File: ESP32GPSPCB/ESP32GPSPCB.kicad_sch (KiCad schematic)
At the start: 11 parts, among them J1 Conn_01x04_Socket, U1 NEO-M8N, U2 W25Q16JVSS, U4 AP2112K-3.3

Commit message: completed GPS and BUCK-BOOST CONV
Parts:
- removed U2: W25Q16JVSS, Package_SO:SOIC-8_5.3x5.3mm_P1.27mm, symbol Memory_Flash:W25Q16JVSS
- added AE1: Antenna, symbol Device:Antenna
- added C4: 470nF, symbol Device:C
- added C5, C6, C7: 10uF, symbol Device:C
- added C8: 100nF, symbol Device:C
- added D2: FIX_IND-LED, symbol Device:LED
- added D3: D, symbol Device:D
- added D4, D5: LED, symbol Device:LED
- added J2: USB_C_Receptacle_USB2.0_14P, symbol Connector:USB_C_Receptacle_USB2.0_14P
- added L1: 27uH, symbol Device:L
- added R10, R11, R3: 1k, symbol Device:R
- added R12: 10mΩ, symbol Device:R
- added R13, R14: 4.7k, symbol Device:R
- added R15: 10K, symbol Device:R
- added R4, R9: 10k, symbol Device:R
- added R5: 22R, symbol Device:R
- added R6, R7: 5.1k, symbol Device:R
- added R8: 2K, symbol Device:R
- added U2: MCP73871-2AA, Package_DFN_QFN:QFN-20-1EP_4x4mm_P0.5mm_EP2.5x2.5mm, symbol Battery_Management:MCP73871-2AA
- added U5: MAX17261xxTD, Package_DFN_QFN:TDFN-14-1EP_3x3mm_P0.4mm_EP1.78x2.35mm, symbol Battery_Management:MAX17261xxTD
- BT1: value Battery_Cell -> CR2032
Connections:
- net +3V3: now also U1.14 (LNA_EN), D3.2 (A), R13.2, R14.2, R15.2, R4.1; no longer R2.2
- net +5V: now also J1.2 (Pin_2), C5.2, C6.2, J2.A4 (VBUS), J2.A9 (VBUS), J2.B4 (VBUS), J2.B9 (VBUS), R10.2, R11.2, R9.2, U2.17 (CE), U2.18 (IN), U2.19 (IN), U2.2 (VPCC), U2.9 (~{TE}); no longer J1.4 (Pin_4)
- net GND: now also U1.7 (VDD_USB), C4.2, C5.1, C6.1, C7.2, C8.1, D2.1 (K), J2.A1 (GND), J2.A12 (GND), J2.B1 (GND), J2.B12 (GND), J2.S1 (SHIELD), R12.1, R6.2, R7.1, R8.1, U2.10 (V_{SS}), U2.11 (V_{SS}), U2.12 (PROG3), U2.21 (V_{SS}), U2.3 (SEL), U2.4 (PROG2), U5.10 (CELLX), U5.15 (GND), U5.3 (SW), U5.8 (GND)
- net at U1.20 (TXD/SPI_MISO): now also J1.4 (Pin_4); no longer J1.2 (Pin_2)
- net at U1.11 (RF_IN): now also AE1.1 (A), L1.2
- net at U1.2 (D_SEL): now also R4.2
- net at U1.3 (TIMEPULSE): now also R3.1
- net at U1.9 (VCC_RF): now also R5.1
- new net: C4.1, U5.11 (REG)
- new net: J2.A5 (CC1), R6.1
- new net: J2.B5 (CC2), R7.2
- new net: R8.2, U2.13 (PROG1)
- new net: R9.1, U2.6 (~{PG})
- new net: D4.1 (K), U2.8 (STAT1/~{LBO})
- new net: D4.2 (A), R11.1
- new net: L1.1, R5.2
- new net: D3.1 (K), R2.2
- new net: R12.2, U5.7 (CSN)
- new net: D2.2 (A), R3.2
- new net: D5.2 (A), R10.1
- new net: D5.1 (K), U2.7 (STAT2)
- new net BAT_ALRT: R15.1, U5.12 (ALRT)
- new net D+: J2.A7 (D-), J2.B7 (D-)
- new net D-: J2.A6 (D+), J2.B6 (D+)
- new net I2C_SCL: R13.1, U5.14 (SCL)
- new net I2C_SDA: R14.1, U5.13 (SDA)
- new net VBAT: C7.1, C8.2, U2.14 (V_{BAT}), U2.15 (V_{BAT}), U2.16 (V_{BAT_SENSE}), U2.5 (THERM), U5.1 (TH), U5.6 (BATT), U5.9 (CSPL)
- new net VSYS: U2.1 (OUT), U2.20 (OUT)
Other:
- note added: "GPS MAPS"
- moved on the sheet: BT1, C1, C2, C3, D1, J1, R1, R2, U1, U4

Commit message: fixed some stuff
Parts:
- added C10, C9: 22uF, symbol Device:C
- added C11: 0.1uF, symbol Device:C
- added C12: 10uF, symbol Device:C
- added J3: Conn_01x14_Socket, symbol Connector:Conn_01x14_Socket
- added J4: Conn_01x04_Socket, symbol Connector:Conn_01x04_Socket
- added L2: 2.2uH, symbol Device:L
- added R16: 100, symbol Device:R
- added U3: TPS63001, Package_SON:Texas_DRC0010J_ThermalVias, symbol Regulator_Switching:TPS63001
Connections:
- net +3V3: now also C10.1, C9.1, J3.1 (Pin_1), J3.8 (Pin_8), U3.1 (VOUT), U3.10 (FB)
- net GND: now also C10.2, C11.2, C12.2, C9.2, J3.2 (Pin_2), U3.11 (PGND), U3.3 (PGND), U3.9 (GND)
- net VSYS: now also C12.1, R16.1, U3.5 (VIN), U3.7 (PS/SYNC)
- new net: C11.1, R16.2, U3.6 (EN), U3.8 (VINA)
- new net: L2.1, U3.2 (L2)
- new net: L2.2, U3.4 (L1)
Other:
- note added: "--"
- note added: "C5,6,7,4,8 Close to IC"
- note added: "CS"
- note added: "DC"
- note added: "GND"
- note added: "LED"
- note added: "RST"
- note added: "SCK"
- note added: "SDI(MOSI)"
- note added: "SDO(MISO)"
- note added: "SD_CS"
- note added: "SD_MISO"
- note added: "SD_MOSI"
- note added: "SD_SCK"
- note added: "TOUCH"
- note added: "T_CLK"
- note added: "T_CS"
- note added: "T_DIN"
- note added: "T_DIO"
- note added: "T_IRQ"
- note added: "VCC"

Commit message: started working on the ESP32 chip
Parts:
- added U6: ESP32-S3-WROOM-1-N16R16VA, RF_Module:ESP32-S3-WROOM-1, symbol RF_Module:ESP32-S3-WROOM-1
- added Y1: Crystal, symbol Device:Crystal
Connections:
- net D+: now also U6.14 (USB_D+)
- net D-: now also U6.13 (USB_D-)
- net GND: now also U6.1 (GND), U6.40 (GND), U6.41 (GND)

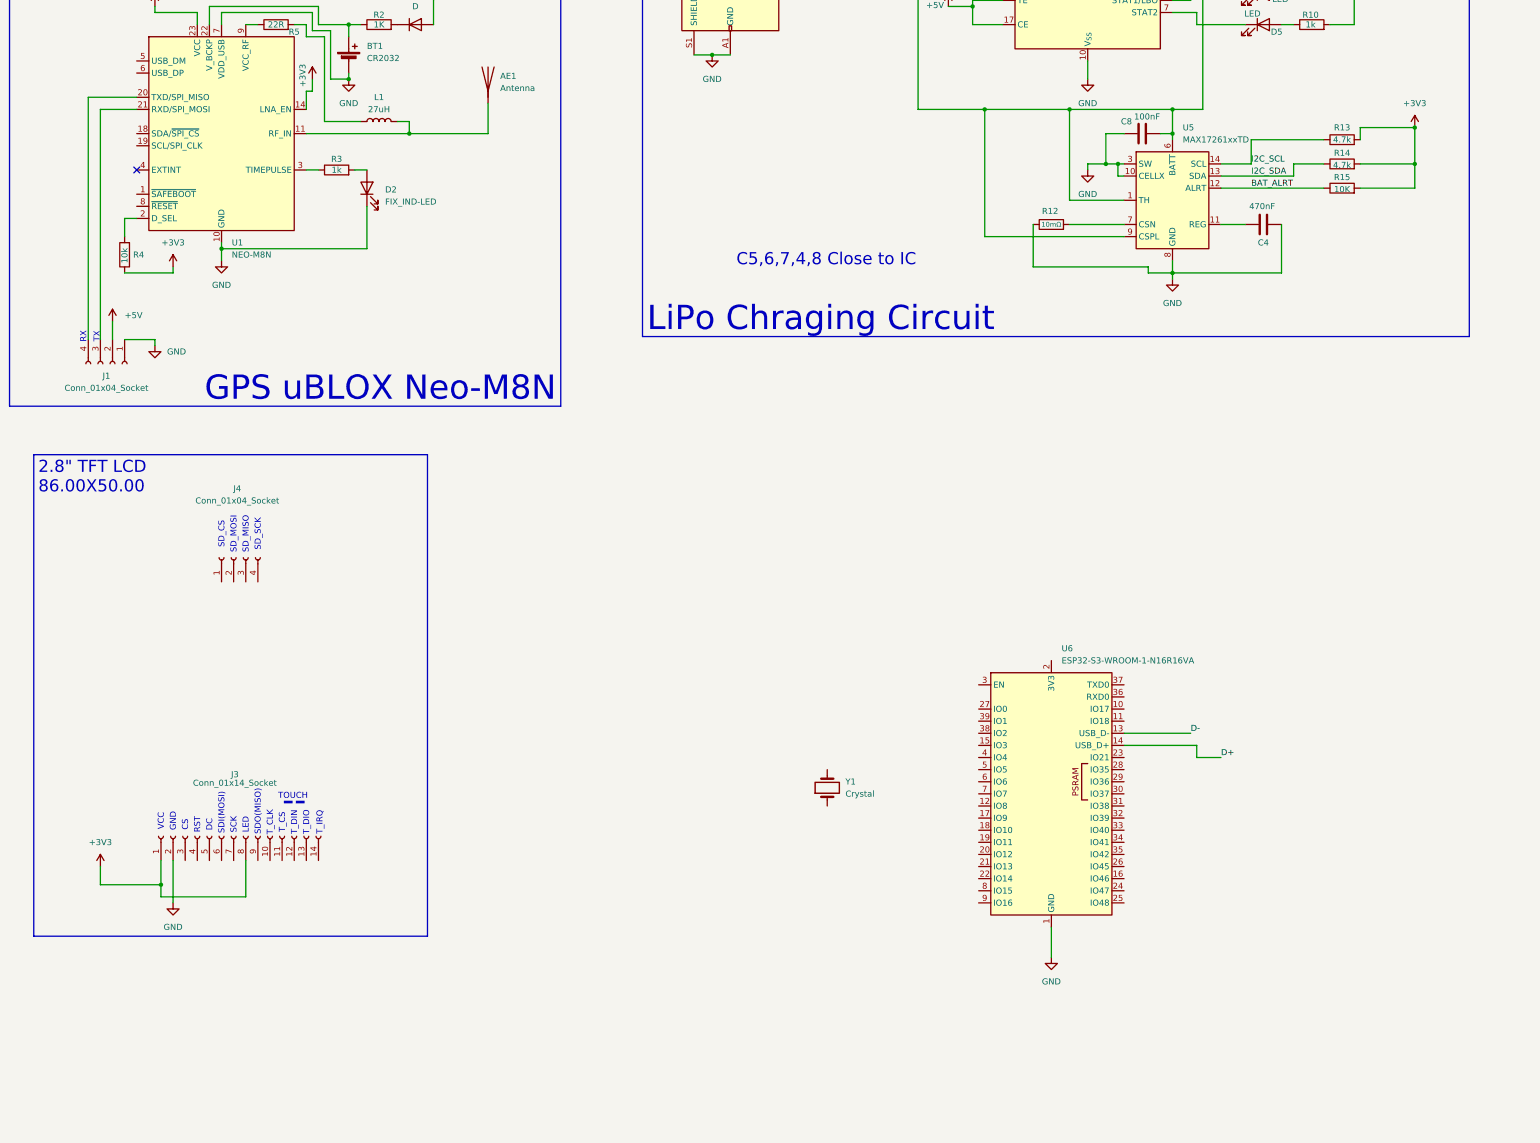
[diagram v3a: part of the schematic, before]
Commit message: completed ESP32 logic, wired up some net labels and stuff
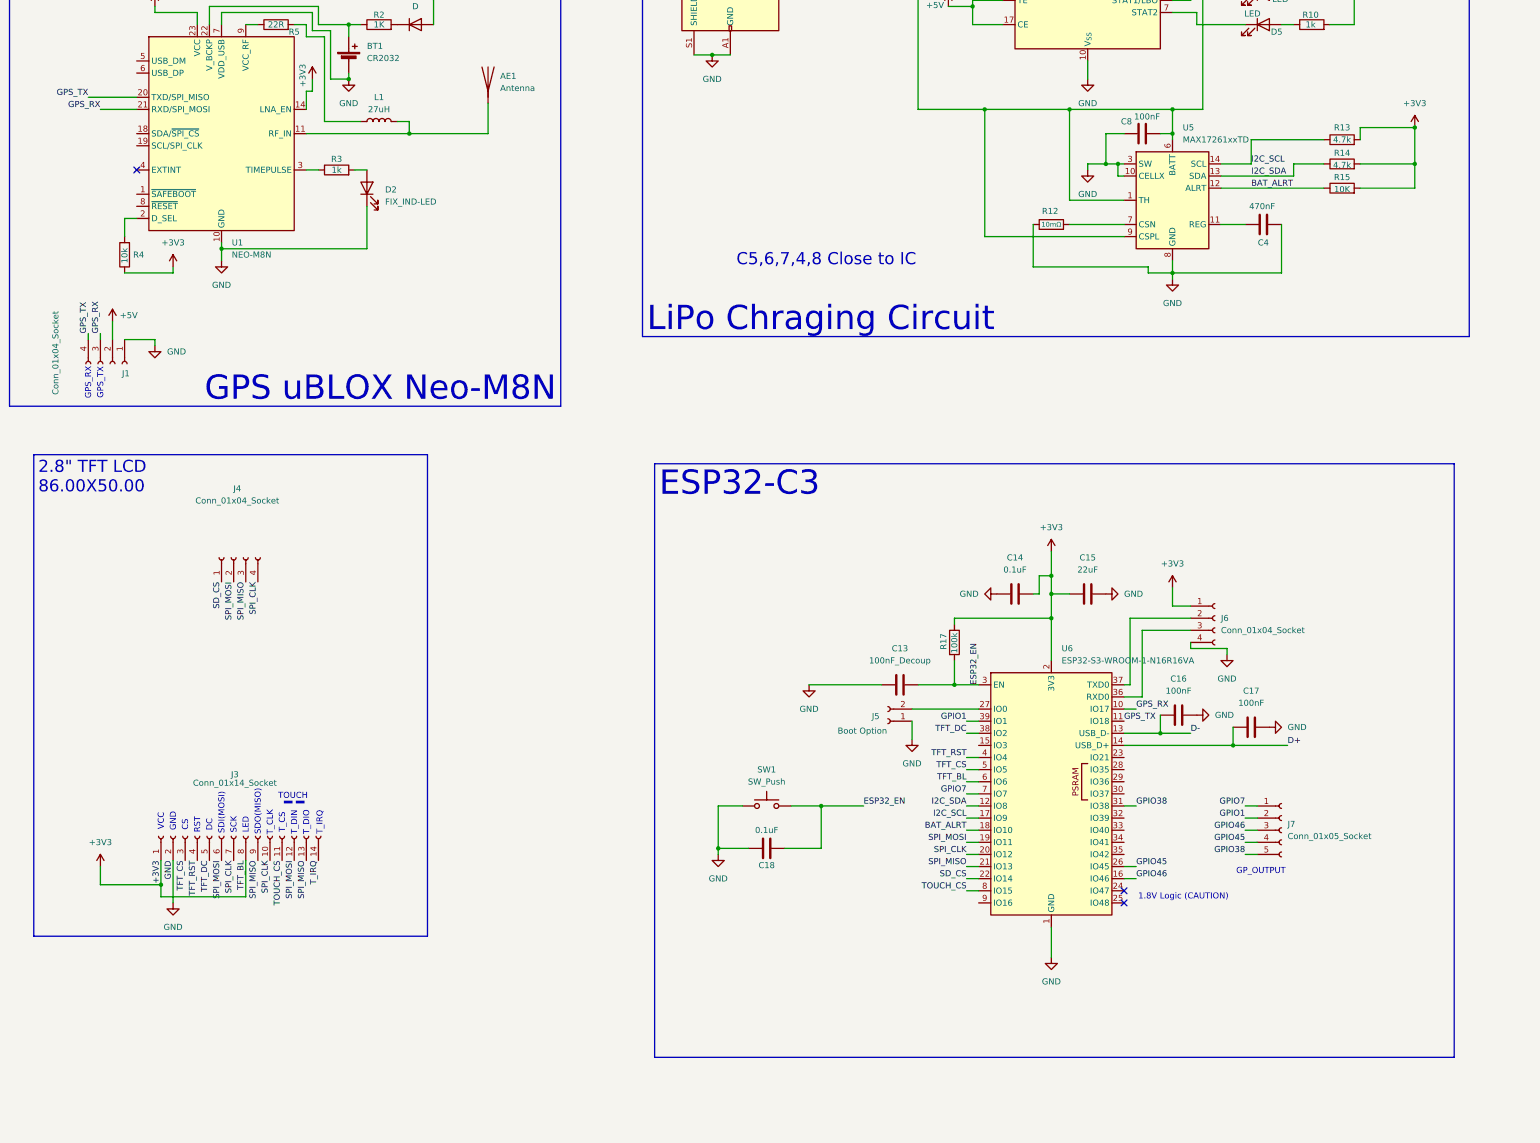
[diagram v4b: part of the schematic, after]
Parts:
- removed Y1: Crystal, symbol Device:Crystal
- added C13: 100nF_Decoup, symbol Device:C
- added C14, C18: 0.1uF, symbol Device:C
- added C15: 22uF, symbol Device:C
- added C16, C17: 100nF, symbol Device:C
- added J5: Boot Option, symbol Connector:Conn_01x02_Socket
- added J6: Conn_01x04_Socket, symbol Connector:Conn_01x04_Socket
- added J7: Conn_01x05_Socket, symbol Connector:Conn_01x05_Socket
- added R17: 100k, symbol Device:R
- added SW1: SW_Push, symbol Switch:SW_Push
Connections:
- net +3V3: now also U6.2 (3V3), U6.6 (IO6), C14.2, C15.1, J6.1 (Pin_1), R17.1
- net BAT_ALRT: now also U6.18 (IO10)
- net D+: now also C17.1
- net D-: now also C16.1
- net GND: now also C13.1, C14.1, C15.2, C16.2, C17.2, C18.2, J5.1 (Pin_1), J6.4 (Pin_4), SW1.1
- net I2C_SCL: now also U6.17 (IO9)
- net I2C_SDA: now also U6.12 (IO8)
- net GPS_RX: now reaches J1.3 (Pin_3), U1.21 (RXD/SPI_MOSI)
- net GPS_RX: now also U6.10 (IO17)
- net GPS_TX: now reaches J1.4 (Pin_4), U1.20 (TXD/SPI_MISO)
- net GPS_TX: now also U6.11 (IO18)
- net GPIO46: now reaches U6.16 (IO46)
- net GPIO46: now also J7.3 (Pin_3)
- net SPI_MOSI: now reaches U6.19 (IO11)
- net SPI_MOSI: now also J3.12 (Pin_12), J3.6 (Pin_6), J4.2 (Pin_2)
- net SPI_CLK: now reaches U6.20 (IO12)
- net SPI_CLK: now also J3.10 (Pin_10), J3.7 (Pin_7), J4.4 (Pin_4)
- net SPI_MISO: now reaches U6.21 (IO13)
- net SPI_MISO: now also J3.13 (Pin_13), J3.9 (Pin_9), J4.3 (Pin_3)
- net SD_CS: now reaches U6.22 (IO14)
- net SD_CS: now also J4.1 (Pin_1)
- net GPIO45: now reaches U6.26 (IO45)
- net GPIO45: now also J7.4 (Pin_4)
- net at U6.27 (IO0): now also J5.2 (Pin_2)
- net ESP32_EN: now reaches U6.3 (EN)
- net ESP32_EN: now also C13.2, C18.1, R17.2, SW1.2
- net GPIO38: now reaches U6.31 (IO38)
- net GPIO38: now also J7.5 (Pin_5)
- net at U6.36 (RXD0): now also J6.3 (Pin_3)
- net at U6.37 (TXD0): now also J6.2 (Pin_2)
- net TFT_DC: now reaches U6.38 (IO2)
- net TFT_DC: now also J3.5 (Pin_5)
- net GPIO1: now reaches U6.39 (IO1)
- net GPIO1: now also J7.2 (Pin_2)
- net TFT_RST: now reaches U6.4 (IO4)
- net TFT_RST: now also J3.4 (Pin_4)
- net TFT_CS: now reaches U6.5 (IO5)
- net TFT_CS: now also J3.3 (Pin_3)
- net GPIO7: now reaches U6.7 (IO7)
- net GPIO7: now also J7.1 (Pin_1)
- net TOUCH_CS: now reaches U6.8 (IO15)
- net TOUCH_CS: now also J3.11 (Pin_11)
- net T_IRQ: now reaches J3.14 (Pin_14)
- no-connect marks 1 -> 3
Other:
- note added: "1.8V Logic (CAUTION)"
- note added: "GPS_RX"
- note added: "GPS_TX"
- note added: "GP_OUTPUT"
- note removed: "RX"
- note removed: "SD_CS"
- note removed: "SD_MISO"
- note removed: "SD_MOSI"
- note removed: "SD_SCK"
- note removed: "TX"

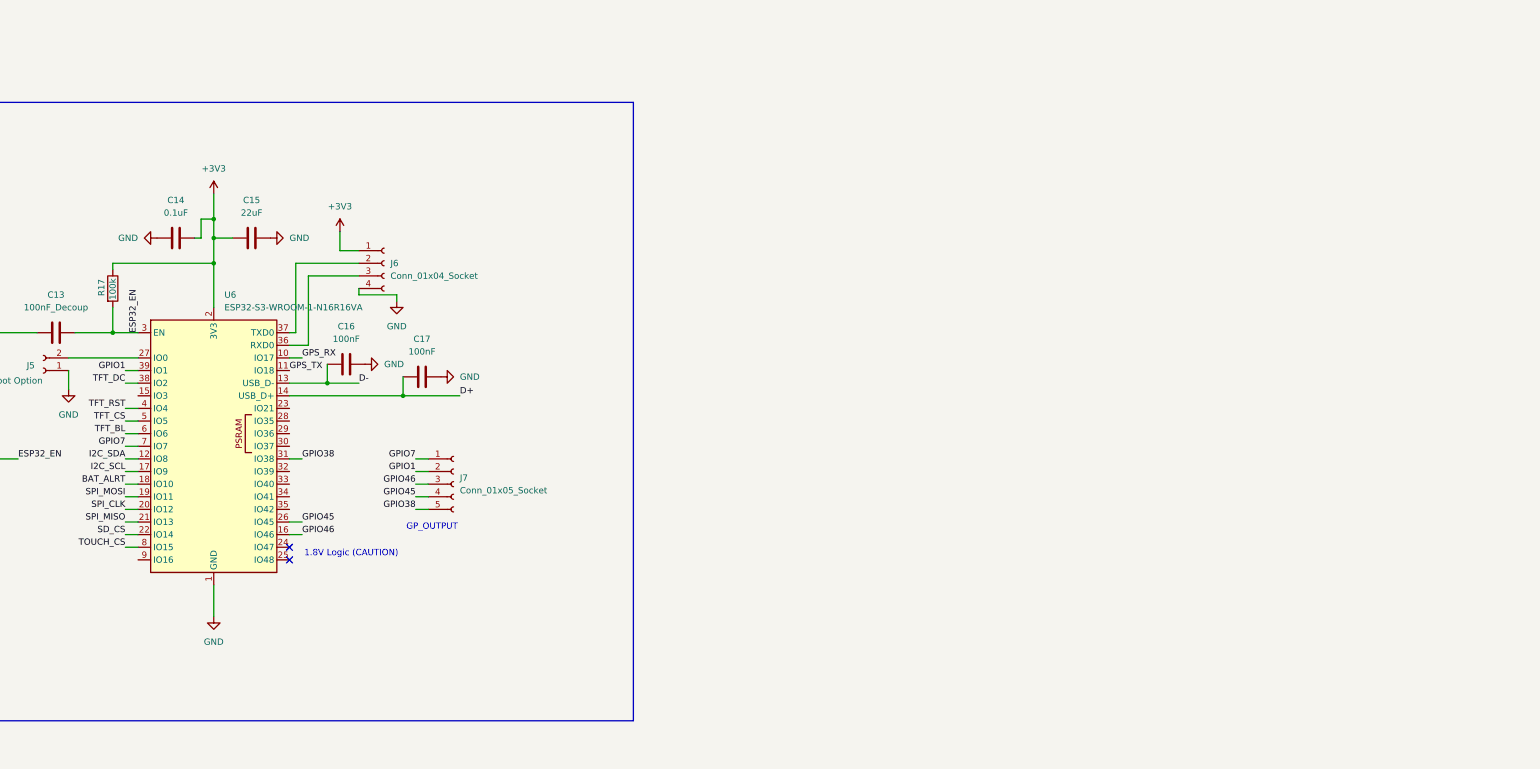
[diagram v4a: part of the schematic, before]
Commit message: completed IMU circuit, added logic level convertor
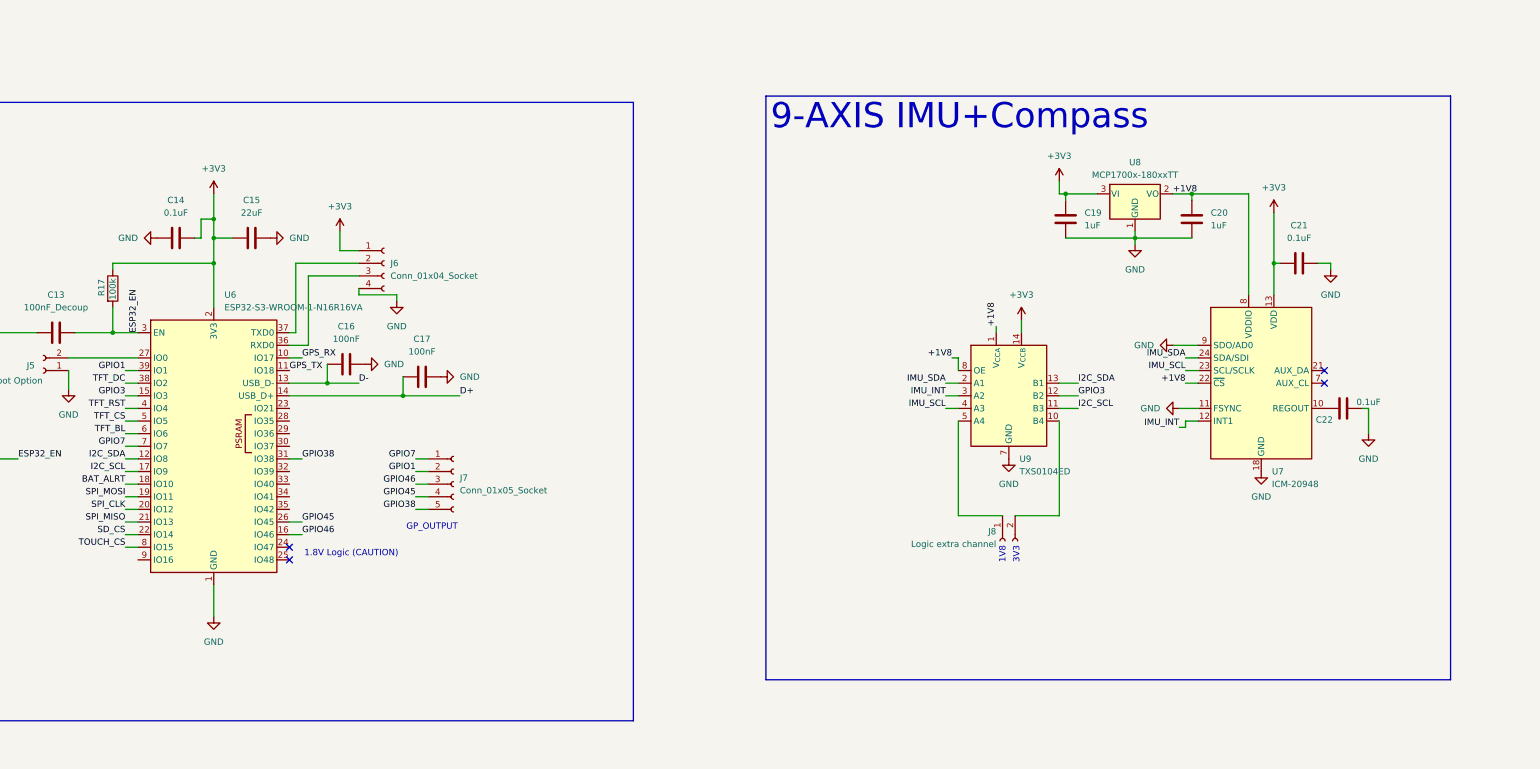
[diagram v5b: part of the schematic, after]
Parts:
- added C19, C20: 1uF, symbol Device:C
- added C21, C22: 0.1uF, symbol Device:C
- added J8: Logic extra channel, symbol Connector:Conn_01x02_Socket
- added U7: ICM-20948, Sensor_Motion:InvenSense_QFN-24_3x3mm_P0.4mm, symbol Sensor_Motion:ICM-20948
- added U8: MCP1700x-180xxTT, Package_TO_SOT_SMD:SOT-23, symbol Regulator_Linear:MCP1700x-180xxTT
- added U9: TXS0104ED, Package_SO:SOIC-14_3.9x8.7mm_P1.27mm, symbol Logic_LevelTranslator:TXS0104ED
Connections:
- net +3V3: now also C19.1, C21.1, U7.13 (VDD), U8.3 (VI), U9.14 (V_{CCB})
- net GND: now also C19.2, C20.2, C21.2, C22.2, U7.11 (FSYNC), U7.18 (GND), U7.20 (GND), U7.9 (SDO/AD0), U8.1 (GND), U9.7 (GND)
- net I2C_SCL: now also U9.11 (B3)
- net I2C_SDA: now also U9.13 (B1)
- net GPIO3: now reaches U6.15 (IO3)
- net GPIO3: now also U9.12 (B2)
- new net: J8.2 (Pin_2), U9.10 (B4)
- new net: J8.1 (Pin_1), U9.5 (A4)
- new net: C22.1, U7.10 (REGOUT)
- new net +1V8: C20.1, U7.22 (~{CS}), U7.8 (VDDIO), U8.2 (VO), U9.1 (V_{CCA}), U9.8 (OE)
- new net IMU_INT: U7.12 (INT1), U9.3 (A2)
- new net IMU_SCL: U7.23 (SCL/SCLK), U9.4 (A3)
- new net IMU_SDA: U7.24 (SDA/SDI), U9.2 (A1)
- no-connect marks 3 -> 5
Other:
- note added: "1V8"
- note added: "3V3"
